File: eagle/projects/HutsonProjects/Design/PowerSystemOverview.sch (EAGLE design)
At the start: 27 parts, among them U1 MCP7384XX, U3 MT3608, U4 LTC3531ES6-3_3

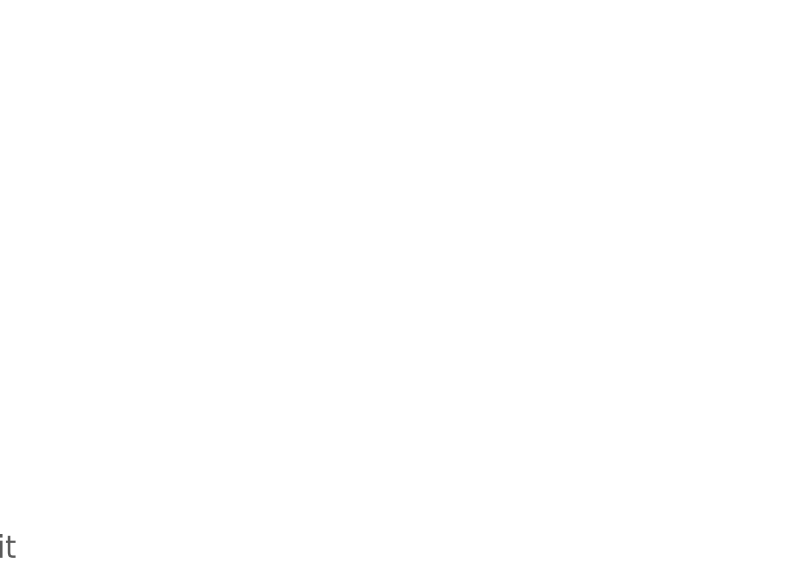
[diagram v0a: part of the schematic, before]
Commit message: Add Resistor Test
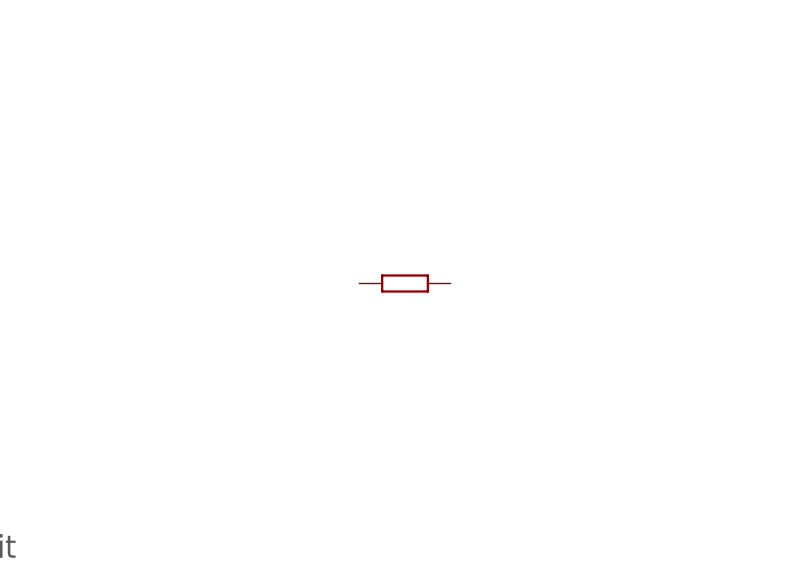
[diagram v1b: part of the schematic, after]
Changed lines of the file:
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@@
 <part name="C7" library="SparkFun-Capacitors" deviceset="2.2UF" device="-0603-10V-20%" value="2.2uF"/>
 <part name="U$4" library="AP910C" deviceset="AP9101C" device=""/>
+<part name="R7" library="docu-dummy" library_urn="urn:adsk.eagle:library:215" deviceset="R" device=""/>
 </parts>
 <sheets>
@@
 <attribute name="VALUE" x="124.46" y="99.06" size="1.778" layer="96"/>
 </instance>
+<instance part="R7" gate="G$1" x="30.48" y="180.34" smashed="yes"/>
 </instances>
 <busses>

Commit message: Added Surface Mount Schottky Diodes to Schematic
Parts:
- removed D1: 1N4148DO35-10, diode:1N4148DO35-10
- removed D2: SMD-DIODE-SCHOTTKY-40V-3A(DO-214AB), SMD-DIODE-SCHOTTKY-40V-3A_DO-214AB_:SMD-DIODE-SCHOTTKY-40V-3A(DO-214AB)
- added U$5, U$6: DB2W31900, DB2W31900L:DB2W31900
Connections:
- removed net N$12: D2.+, L1.2, U3.SW
- new net N$17: C6.1, R5.2, U$6.CATHODE
- new net N$18: L1.2, U$6.ANODE, U3.SW
- net CONT_ON_SOLENOID: now also U$5.ANODE; no longer C6.1, D1.A, D2.-, R5.2
- net N$3: now also U$5.CATHODE; no longer D1.C
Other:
- moved on the sheet: C6, R5, R6

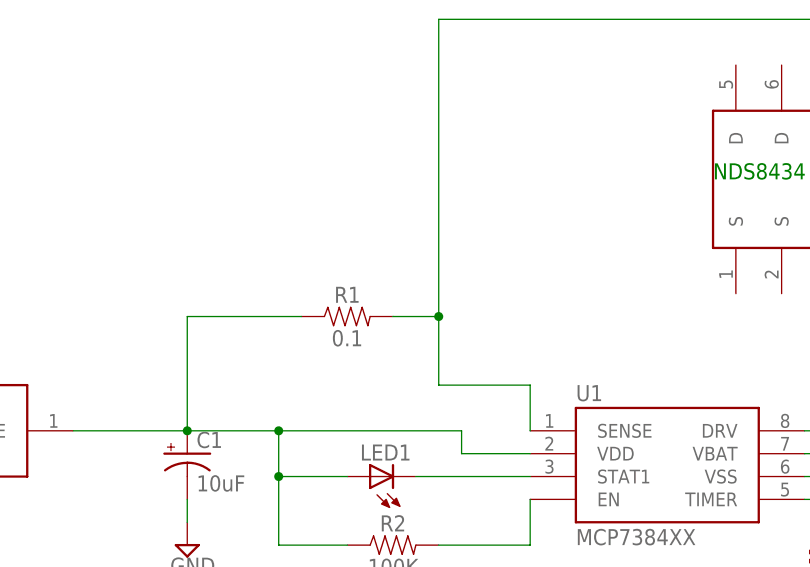
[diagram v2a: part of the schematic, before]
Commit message: Added 0.1mohm chip resistor
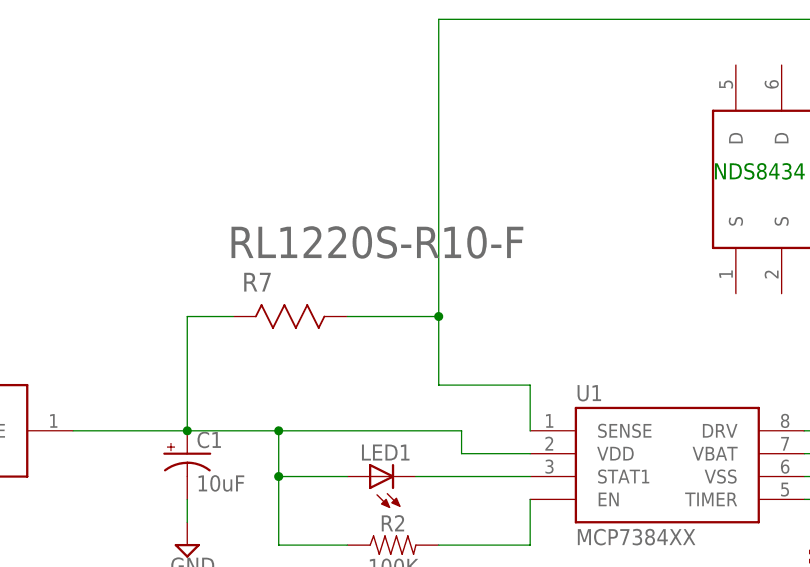
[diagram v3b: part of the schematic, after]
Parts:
- removed R1: 0.1, SparkFun-Resistors:0.1OHM-1210-1/2W-1%
- added R7: RL1220S-R10-F, RL1220S-R10-F:RL1220S-R10-F
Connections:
- net N$1: now also R7.R1; no longer R1.2
- net N$3: now also R7.R2; no longer R1.1
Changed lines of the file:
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@@
 <part name="P+1" library="supply1" library_urn="urn:adsk.eagle:library:371" deviceset="+5V" device=""/>
 <part name="C1" library="SparkFun-Capacitors" deviceset="10UF-POLAR" device="-0603-6.3V-20%(TANT)" value="10uF"/>
-<part name="R1" library="SparkFun-Resistors" deviceset="0.1OHM" device="-1210-1/2W-1%" value="0.1"/>
 <part name="SUPPLY1" library="supply2" library_urn="urn:adsk.eagle:library:372" deviceset="GND" device=""/>
 <part name="SUPPLY2" library="supply2" library_urn="urn:adsk.eagle:library:372" deviceset="GND" device=""/>
@@
 <part name="U$5" library="DB2W31900L" deviceset="DB2W31900" device=""/>
 <part name="U$6" library="DB2W31900L" deviceset="DB2W31900" device=""/>
+<part name="R7" library="RL1220S-R10-F" deviceset="RL1220S-R10-F" device=""/>
 </parts>
 <sheets>
@@
 <attribute name="VALUE" x="-11.684" y="87.249" size="1.778" layer="96" font="vector"/>
 </instance>
-<instance part="R1" gate="G$1" x="5.08" y="106.68" smashed="yes">
-<attribute name="NAME" x="5.08" y="108.204" size="1.778" layer="95" font="vector" align="bottom-center"/>
-<attribute name="VALUE" x="5.08" y="105.156" size="1.778" layer="96" font="vector" align="top-center"/>
-</instance>
 <instance part="SUPPLY1" gate="GND" x="-12.7" y="81.28" smashed="yes">
 <attribute name="VALUE" x="-14.605" y="78.105" size="1.778" layer="96"/>
@@
 <instance part="U$5" gate="G$1" x="-48.26" y="93.98" smashed="yes" rot="R90"/>
 <instance part="U$6" gate="G$1" x="231.14" y="152.4" smashed="yes" rot="R90"/>
+<instance part="R7" gate="A" x="-7.62" y="106.68" smashed="yes">
+<attribute name="VALUE" x="-8.20755" y="113.173040625" size="3.48353125" layer="96" ratio="10" rot="SR0"/>
+<attribute name="NAME" x="-6.628359375" y="109.451509375" size="2.084990625" layer="95" ratio="10" rot="SR0"/>
+</instance>
 </instances>
 <busses>
@@
 <wire x1="-12.7" y1="93.98" x2="-12.7" y2="106.68" width="0.1524" layer="91"/>
 <junction x="-12.7" y="93.98"/>
-<pinref part="R1" gate="G$1" pin="1"/>
-<wire x1="-12.7" y1="106.68" x2="0" y2="106.68" width="0.1524" layer="91"/>
 <wire x1="-12.7" y1="93.98" x2="-2.54" y2="93.98" width="0.1524" layer="91"/>
 <wire x1="-2.54" y1="93.98" x2="-2.54" y2="88.9" width="0.1524" layer="91"/>
@@
 <pinref part="U$5" gate="G$1" pin="CATHODE"/>
 <wire x1="-25.4" y1="93.98" x2="-12.7" y2="93.98" width="0.1524" layer="91"/>
+<pinref part="R7" gate="A" pin="R2"/>
+<wire x1="-12.7" y1="106.68" x2="-7.62" y2="106.68" width="0.1524" layer="91"/>
 </segment>
 </net>
@@
 <net name="N$1" class="0">
 <segment>
-<pinref part="R1" gate="G$1" pin="2"/>
-<wire x1="10.16" y1="106.68" x2="15.24" y2="106.68" width="0.1524" layer="91"/>
 <pinref part="U1" gate="G$1" pin="SENSE"/>
 <wire x1="25.4" y1="93.98" x2="25.4" y2="99.06" width="0.1524" layer="91"/>
@@
 <wire x1="15.24" y1="139.7" x2="63.5" y2="139.7" width="0.1524" layer="91"/>
 <junction x="15.24" y="106.68"/>
-</segment>
-</net>
+<pinref part="R7" gate="A" pin="R1"/>
+<wire x1="5.08" y1="106.68" x2="15.24" y2="106.68" width="0.1524" layer="91"/>
+</segment>
+</net>

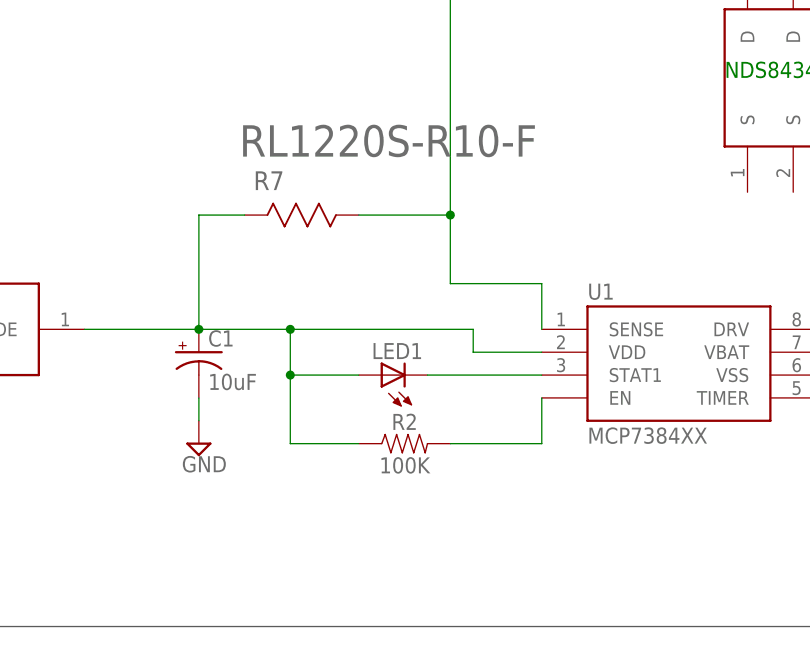
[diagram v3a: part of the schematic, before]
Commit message: 100kohm chip resistor created
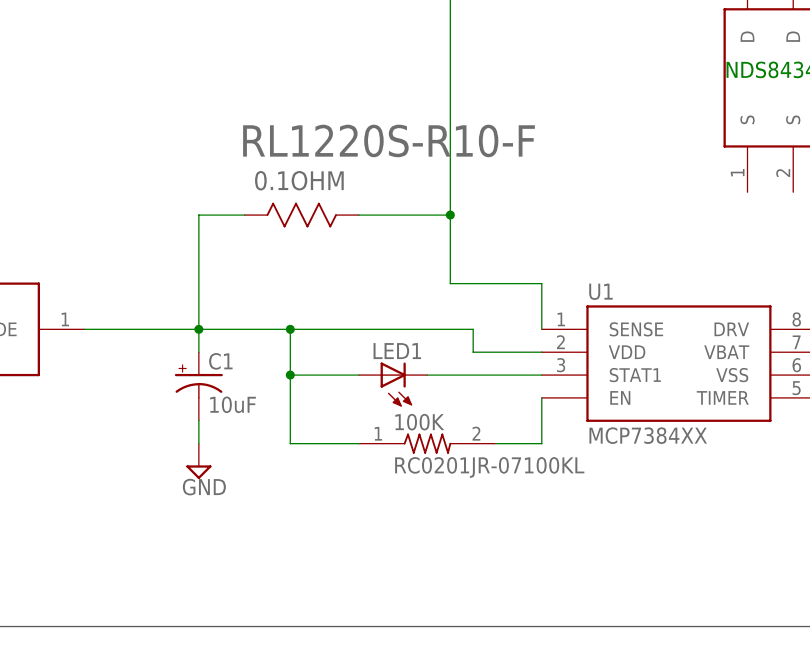
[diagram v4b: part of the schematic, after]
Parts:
- removed R2: 100K, SparkFun-Resistors:100KOHM-0402-1/16W-1%
- added 100K: RC0201JR-07100KL, RC0201JR-07100KL:RC0201JR-07100KL
- renumbered R7 to 0.1OHM
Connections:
- net N$3: now also 100K.1; no longer R2.1
- net N$4: now also 100K.2; no longer R2.2
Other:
- moved on the sheet: C1
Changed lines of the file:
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@@
 <part name="SUPPLY3" library="supply2" library_urn="urn:adsk.eagle:library:372" deviceset="GND" device=""/>
 <part name="LED1" library="eagle-ltspice" library_urn="urn:adsk.eagle:library:217" deviceset="LED_E" device="SML0603" package3d_urn="urn:adsk.eagle:package:13315/1"/>
-<part name="R2" library="SparkFun-Resistors" deviceset="100KOHM" device="-0402-1/16W-1%" value="100K"/>
 <part name="C2" library="SparkFun-Capacitors" deviceset="10UF-POLAR" device="-0603-6.3V-20%(TANT)" value="10uF"/>
 <part name="C3" library="SparkFun-Capacitors" deviceset="0.1UF" device="-0402-16V-10%" value="0.1uF"/>
@@
 <part name="U$5" library="DB2W31900L" deviceset="DB2W31900" device=""/>
 <part name="U$6" library="DB2W31900L" deviceset="DB2W31900" device=""/>
-<part name="R7" library="RL1220S-R10-F" deviceset="RL1220S-R10-F" device=""/>
+<part name="0.1OHM" library="RL1220S-R10-F" deviceset="RL1220S-R10-F" device=""/>
+<part name="100K" library="RC0201JR-07100KL" deviceset="RC0201JR-07100KL" device=""/>
 </parts>
 <sheets>
@@
 <attribute name="VALUE" x="-104.14" y="109.22" size="1.778" layer="96"/>
 </instance>
-<instance part="C1" gate="G$1" x="-12.7" y="91.44" smashed="yes">
-<attribute name="NAME" x="-11.684" y="92.075" size="1.778" layer="95" font="vector"/>
-<attribute name="VALUE" x="-11.684" y="87.249" size="1.778" layer="96" font="vector"/>
-</instance>
-<instance part="SUPPLY1" gate="GND" x="-12.7" y="81.28" smashed="yes">
-<attribute name="VALUE" x="-14.605" y="78.105" size="1.778" layer="96"/>
+<instance part="C1" gate="G$1" x="-12.7" y="88.9" smashed="yes">
+<attribute name="NAME" x="-11.684" y="89.535" size="1.778" layer="95" font="vector"/>
+<attribute name="VALUE" x="-11.684" y="84.709" size="1.778" layer="96" font="vector"/>
+</instance>
+<instance part="SUPPLY1" gate="GND" x="-12.7" y="78.74" smashed="yes">
+<attribute name="VALUE" x="-14.605" y="75.565" size="1.778" layer="96"/>
 </instance>
 <instance part="SUPPLY2" gate="GND" x="58.42" y="71.12" smashed="yes">
@@
 <attribute name="NAME" x="12.192" y="92.456" size="1.778" layer="95" rot="R180"/>
 <attribute name="VALUE" x="12.192" y="94.615" size="1.778" layer="96" rot="R180"/>
-</instance>
-<instance part="R2" gate="G$1" x="10.16" y="81.28" smashed="yes">
-<attribute name="NAME" x="10.16" y="82.804" size="1.778" layer="95" font="vector" align="bottom-center"/>
-<attribute name="VALUE" x="10.16" y="79.756" size="1.778" layer="96" font="vector" align="top-center"/>
 </instance>
 <instance part="C2" gate="G$1" x="76.2" y="86.36" smashed="yes">
@@
 <instance part="U$5" gate="G$1" x="-48.26" y="93.98" smashed="yes" rot="R90"/>
 <instance part="U$6" gate="G$1" x="231.14" y="152.4" smashed="yes" rot="R90"/>
-<instance part="R7" gate="A" x="-7.62" y="106.68" smashed="yes">
+<instance part="0.1OHM" gate="A" x="-7.62" y="106.68" smashed="yes">
 <attribute name="VALUE" x="-8.20755" y="113.173040625" size="3.48353125" layer="96" ratio="10" rot="SR0"/>
 <attribute name="NAME" x="-6.628359375" y="109.451509375" size="2.084990625" layer="95" ratio="10" rot="SR0"/>
+</instance>
+<instance part="100K" gate="G$1" x="12.7" y="81.28" smashed="yes">
+<attribute name="NAME" x="8.89" y="82.7786" size="1.778" layer="95"/>
+<attribute name="VALUE" x="8.89" y="77.978" size="1.778" layer="96"/>
 </instance>
 </instances>
@@
 <net name="N$3" class="0">
 <segment>
-<pinref part="C1" gate="G$1" pin="+"/>
-<wire x1="-12.7" y1="93.98" x2="-12.7" y2="106.68" width="0.1524" layer="91"/>
-<junction x="-12.7" y="93.98"/>
-<wire x1="-12.7" y1="93.98" x2="-2.54" y2="93.98" width="0.1524" layer="91"/>
 <wire x1="-2.54" y1="93.98" x2="-2.54" y2="88.9" width="0.1524" layer="91"/>
 <pinref part="LED1" gate="G$1" pin="A"/>
@@
 <wire x1="-2.54" y1="88.9" x2="-2.54" y2="81.28" width="0.1524" layer="91"/>
 <junction x="-2.54" y="88.9"/>
-<pinref part="R2" gate="G$1" pin="1"/>
-<wire x1="-2.54" y1="81.28" x2="5.08" y2="81.28" width="0.1524" layer="91"/>
 <wire x1="-2.54" y1="93.98" x2="17.78" y2="93.98" width="0.1524" layer="91"/>
 <wire x1="17.78" y1="93.98" x2="17.78" y2="91.44" width="0.1524" layer="91"/>
-<junction x="-2.54" y="93.98"/>
 <pinref part="U1" gate="G$1" pin="VDD"/>
 <wire x1="17.78" y1="91.44" x2="25.4" y2="91.44" width="0.1524" layer="91"/>
+<pinref part="0.1OHM" gate="A" pin="R2"/>
+<wire x1="-12.7" y1="106.68" x2="-7.62" y2="106.68" width="0.1524" layer="91"/>
+<pinref part="C1" gate="G$1" pin="+"/>
+<wire x1="-12.7" y1="91.44" x2="-12.7" y2="93.98" width="0.1524" layer="91"/>
 <pinref part="U$5" gate="G$1" pin="CATHODE"/>
+<wire x1="-12.7" y1="93.98" x2="-12.7" y2="106.68" width="0.1524" layer="91"/>
 <wire x1="-25.4" y1="93.98" x2="-12.7" y2="93.98" width="0.1524" layer="91"/>
-<pinref part="R7" gate="A" pin="R2"/>
-<wire x1="-12.7" y1="106.68" x2="-7.62" y2="106.68" width="0.1524" layer="91"/>
+<junction x="-12.7" y="93.98"/>
+<wire x1="-2.54" y1="93.98" x2="-12.7" y2="93.98" width="0.1524" layer="91"/>
+<junction x="-2.54" y="93.98"/>
+<pinref part="100K" gate="G$1" pin="1"/>
+<wire x1="-2.54" y1="81.28" x2="5.08" y2="81.28" width="0.1524" layer="91"/>
 </segment>
 </net>
@@
 <pinref part="C1" gate="G$1" pin="-"/>
 <pinref part="SUPPLY1" gate="GND" pin="GND"/>
-<wire x1="-12.7" y1="86.36" x2="-12.7" y2="83.82" width="0.1524" layer="91"/>
+<wire x1="-12.7" y1="83.82" x2="-12.7" y2="81.28" width="0.1524" layer="91"/>
 </segment>
 <segment>
@@
 <net name="N$4" class="0">
 <segment>
-<pinref part="R2" gate="G$1" pin="2"/>
-<wire x1="15.24" y1="81.28" x2="25.4" y2="81.28" width="0.1524" layer="91"/>
 <pinref part="U1" gate="G$1" pin="EN"/>
 <wire x1="25.4" y1="81.28" x2="25.4" y2="86.36" width="0.1524" layer="91"/>
+<pinref part="100K" gate="G$1" pin="2"/>
+<wire x1="20.32" y1="81.28" x2="25.4" y2="81.28" width="0.1524" layer="91"/>
 </segment>
 </net>
@@
 <wire x1="15.24" y1="139.7" x2="63.5" y2="139.7" width="0.1524" layer="91"/>
 <junction x="15.24" y="106.68"/>
-<pinref part="R7" gate="A" pin="R1"/>
+<pinref part="0.1OHM" gate="A" pin="R1"/>
 <wire x1="5.08" y1="106.68" x2="15.24" y2="106.68" width="0.1524" layer="91"/>
 </segment>
